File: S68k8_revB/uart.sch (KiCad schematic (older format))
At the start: 12 parts, among them J3 Conn_02x05_Top_Bottom, J4 Conn_02x05_Top_Bottom, U10 MC68681P, U18 MC1488, U19 MC1489, Y3 3.6864M

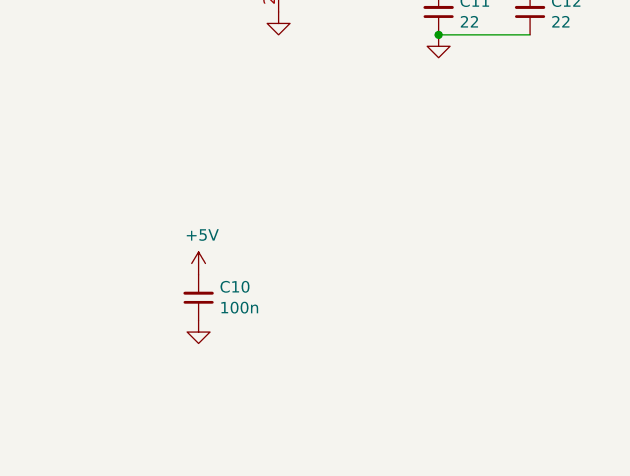
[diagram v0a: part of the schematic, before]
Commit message: S68k8: moved copper pours for power distribution to the bottom layer
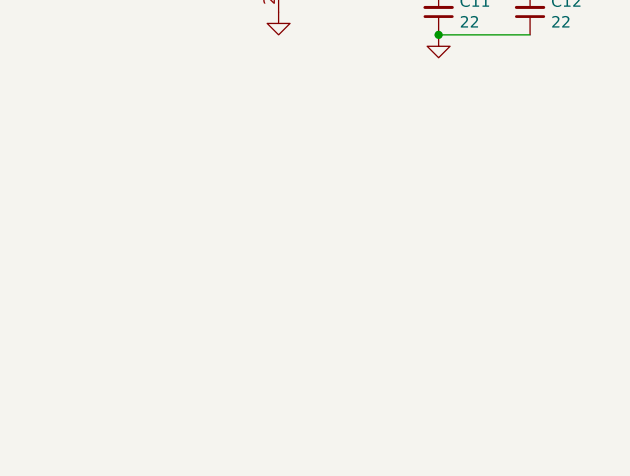
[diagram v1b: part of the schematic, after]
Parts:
- removed C10: 100n, Capacitor_THT:C_Rect_L7.0mm_W2.0mm_P5.00mm, symbol Device:C_Small
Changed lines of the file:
@@
 	-1   0    0    1
-$EndComp
-$Comp
-L Device:C_Small C10
-U 1 1 60115BD1
-P 2450 5050
-F 0 "C10" H 2358 5004 50  0000 R CNN
-F 1 "100n" H 2358 5095 50  0000 R CNN
-F 2 "Capacitor_THT:C_Rect_L7.0mm_W2.0mm_P5.00mm" H 2450 5050 50  0001 C CNN
-F 3 "~" H 2450 5050 50  0001 C CNN
-	1    2450 5050
-	-1   0    0    1
-$EndComp
-$Comp
-L power:+5V #PWR049
-U 1 1 6011BF37
-P 2450 4950
-F 0 "#PWR049" H 2450 4800 50  0001 C CNN
-F 1 "+5V" H 2465 5123 50  0000 C CNN
-F 2 "" H 2450 4950 50  0001 C CNN
-F 3 "" H 2450 4950 50  0001 C CNN
-	1    2450 4950
-	1    0    0    -1
-$EndComp
-$Comp
-L power:GND #PWR050
-U 1 1 6011C2DB
-P 2450 5150
-F 0 "#PWR050" H 2450 4900 50  0001 C CNN
-F 1 "GND" V 2455 5022 50  0001 R CNN
-F 2 "" H 2450 5150 50  0001 C CNN
-F 3 "" H 2450 5150 50  0001 C CNN
-	1    2450 5150
-	1    0    0    -1
 $EndComp
 Text Label 3800 1750 2    50   ~ 0
